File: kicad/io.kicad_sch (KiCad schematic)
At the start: 11 parts, among them J2 UART, P1 Mini-DIN_6pins_ver3, U13 uSD adapter, U14 8259, U16 16550

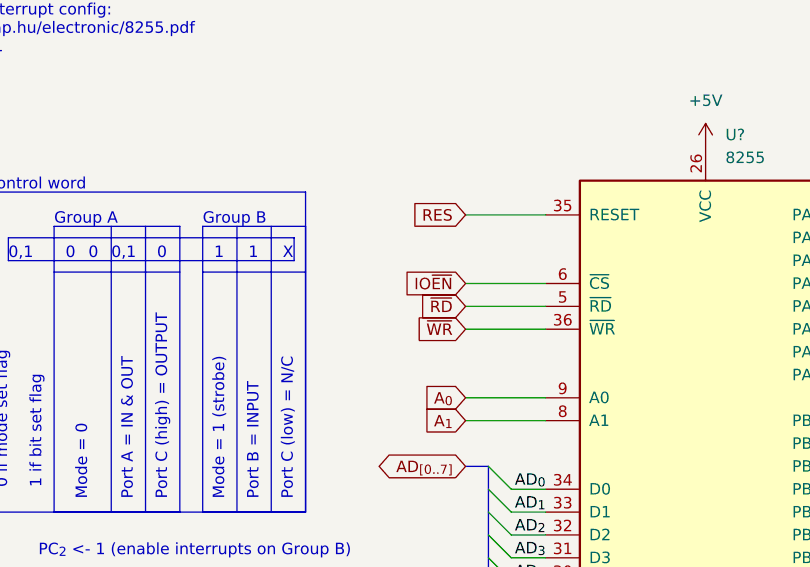
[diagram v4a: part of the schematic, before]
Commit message: 135x160 board
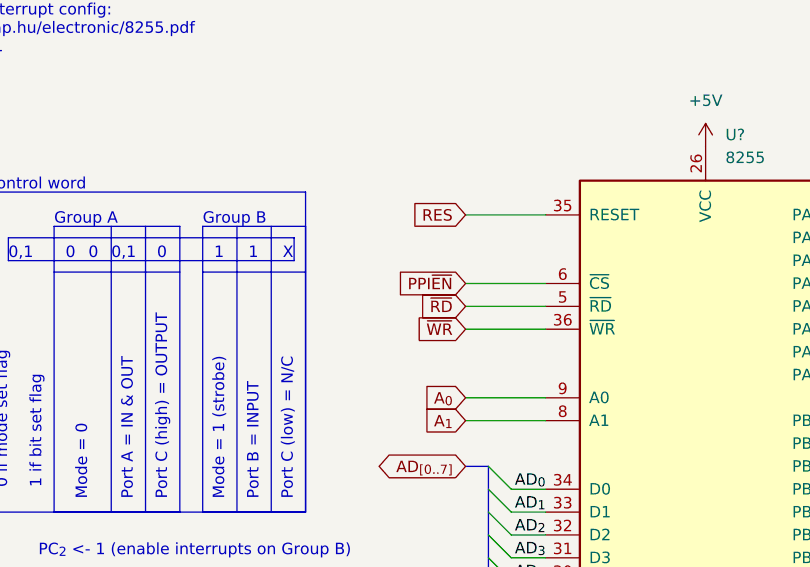
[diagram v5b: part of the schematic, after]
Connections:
- net IO~{EN} renamed PPI~{EN}
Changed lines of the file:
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@@
     )
   )
-  (global_label "IO~{EN}" (shape input) (at 196.85 55.88 180) (fields_autoplaced)
-    (effects (font (size 1.27 1.27)) (justify right))
-    (property "Intersheetrefs" "${INTERSHEET_REFS}" (at 189.45 55.88 0)
+  (global_label "PPI~{EN}" (shape input) (at 196.85 55.88 180) (fields_autoplaced)
+    (effects (font (size 1.27 1.27)) (justify right))
+    (property "Intersheetrefs" "${INTERSHEET_REFS}" (at 188.2405 55.88 0)
       (effects (font (size 1.27 1.27)) (justify right) hide)
     )
@@
       (effects (font (size 1.27 1.27)) hide)
     )
-    (property "Datasheet" "" (at 269.24 81.28 0)
-      (effects (font (size 1.27 1.27)) hide)
-    )
+    (property "Datasheet" "https://cdn-shop.adafruit.com/datasheets/WS0010.pdf" (at 269.24 81.28 0)
+      (effects (font (size 1.27 1.27)) hide)
+    )

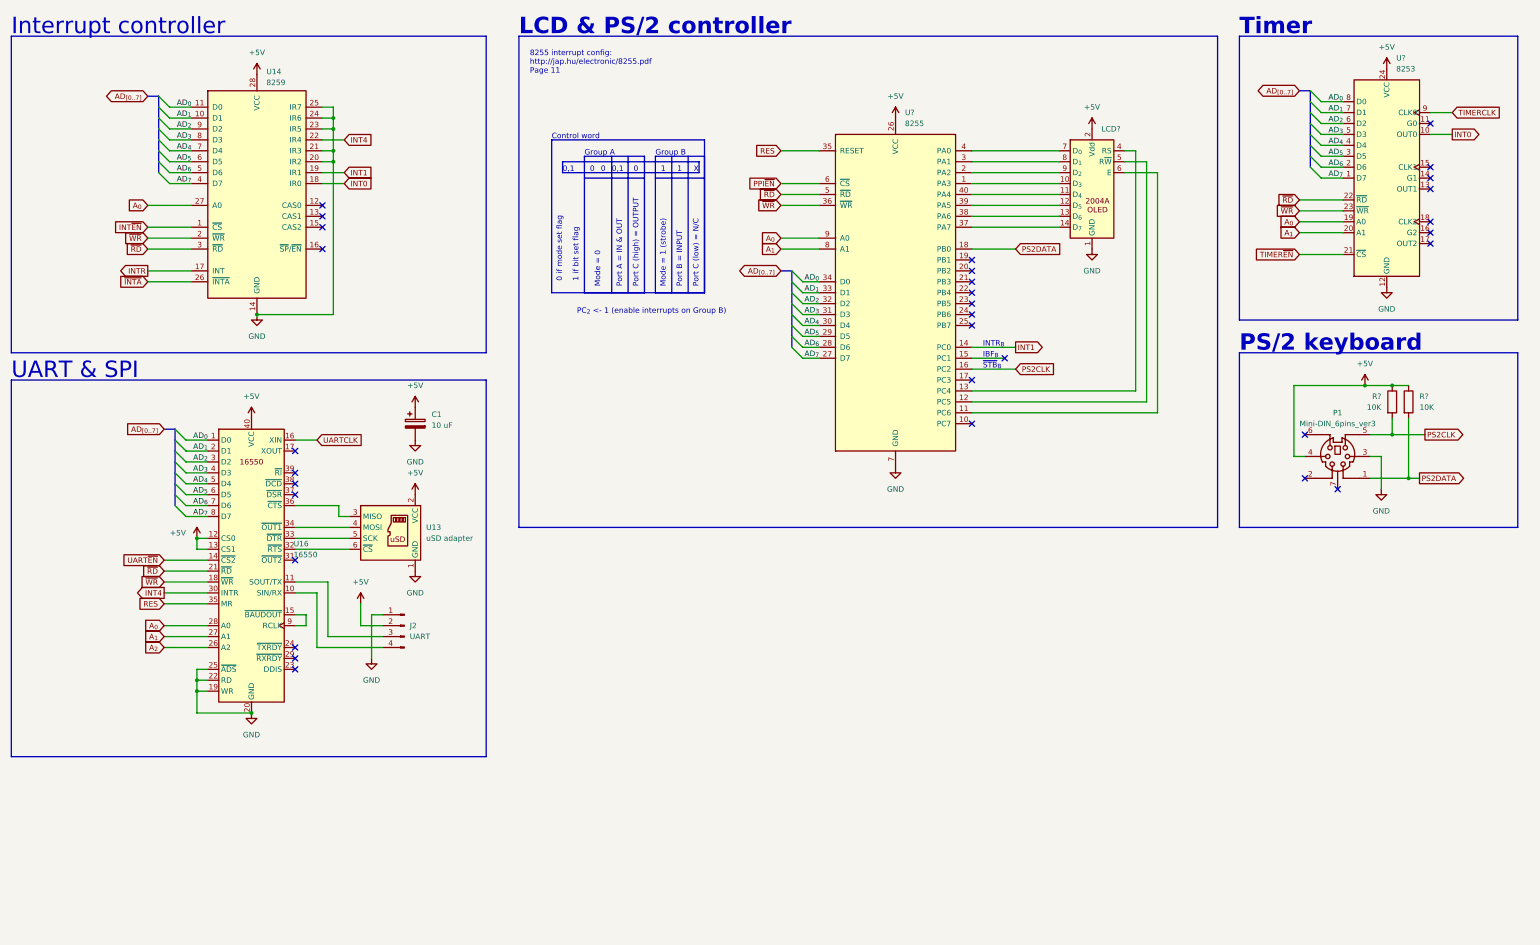
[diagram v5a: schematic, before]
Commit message: Add second GAL
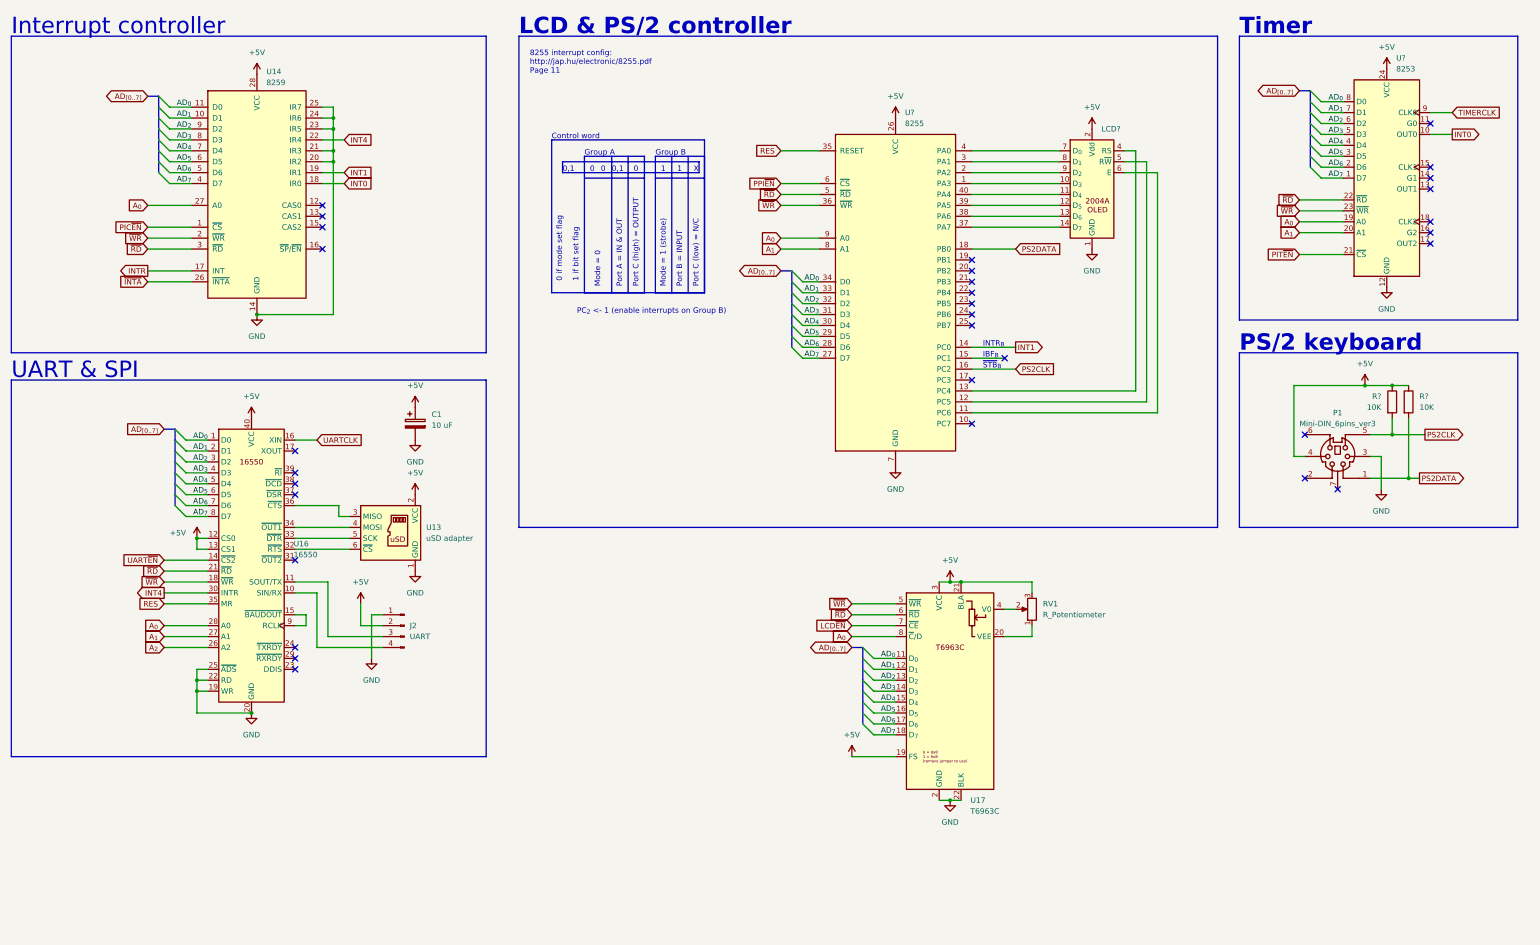
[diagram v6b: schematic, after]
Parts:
- added RV1: R_Potentiometer, symbol Device:R_Potentiometer
- added U17: T6963C, symbol lcd:24064-LCD
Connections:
- net +5V: now also RV1.3, U17.19 (FS), U17.21 (BLA), U17.3 (VCC)
- net AD_{0}: now also U17.11 (D_{0})
- net AD_{1}: now also U17.12 (D_{1})
- net AD_{2}: now also U17.13 (D_{2})
- net AD_{3}: now also U17.14 (D_{3})
- net AD_{4}: now also U17.15 (D_{4})
- net AD_{5}: now also U17.16 (D_{5})
- net AD_{6}: now also U17.17 (D_{6})
- net AD_{7}: now also U17.18 (D_{7})
- net A_{0}: now also U17.8 (~{C}/D)
- net GND: now also U17.2 (GND), U17.22 (BLK)
- net ~{RD}: now also U17.6 (~{RD})
- net ~{WR}: now also U17.5 (~{WR})
- net INT~{EN} renamed PIC~{EN}
- net TIMER~{EN} renamed PIT~{EN}
- new net: RV1.1, U17.20 (VEE)
- new net: RV1.2, U17.4 (V0)
- new net LCD~{EN}: U17.7 (~{CE})

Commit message: PCB 2.0 RC
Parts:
- removed C1: 10 uF, Capacitor_THT:CP_Radial_D6.3mm_P2.50mm, symbol Device:C_Polarized
- removed LCD?: ~, footprints:2004A-OLED, symbol lcd:2004A-OLED
- RV1: footprint (none) -> Potentiometer_THT:Potentiometer_Bourns_3296Y_Vertical
- U17: footprint (none) -> footprints:LCD24064
- U?: footprint Package_DIP:DIP-40_W15.24mm_Socket -> Package_DIP:DIP-40_W15.24mm
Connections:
- no-connect marks 32 -> 43
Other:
- note added: "PS/2 controller"
- note removed: "LCD & PS/2 controller"

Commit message: Final PCB
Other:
- note added: "240x64 LCD (40x08)"
- moved on the sheet: RV1, U17
